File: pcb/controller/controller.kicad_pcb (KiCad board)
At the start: 2 copper layers, 100 x 40 mm, 27 parts, among them J1 Conn_01x02, J10 USB_C_Receptacle_USB2.0_16P, J2 Conn_01x02, J3 Conn_01x02, J4 Conn_01x02, J5 Conn_01x02, J6 Conn_01x02, J7 Conn_01x02, J8 RJ45, U2 AP2112K-3.3

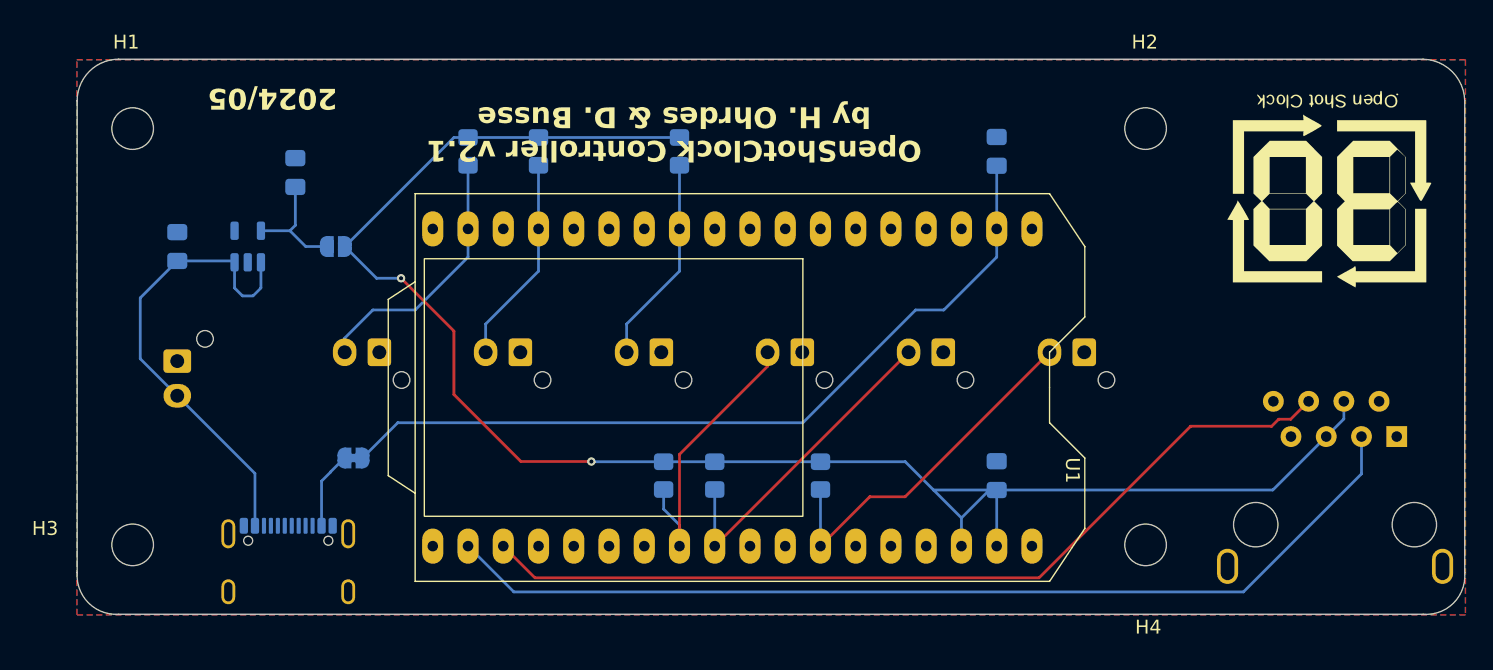
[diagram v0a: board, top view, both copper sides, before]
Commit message: fix missing 5V connection in controller PCB, when USB-C is not used, bump to v2.2
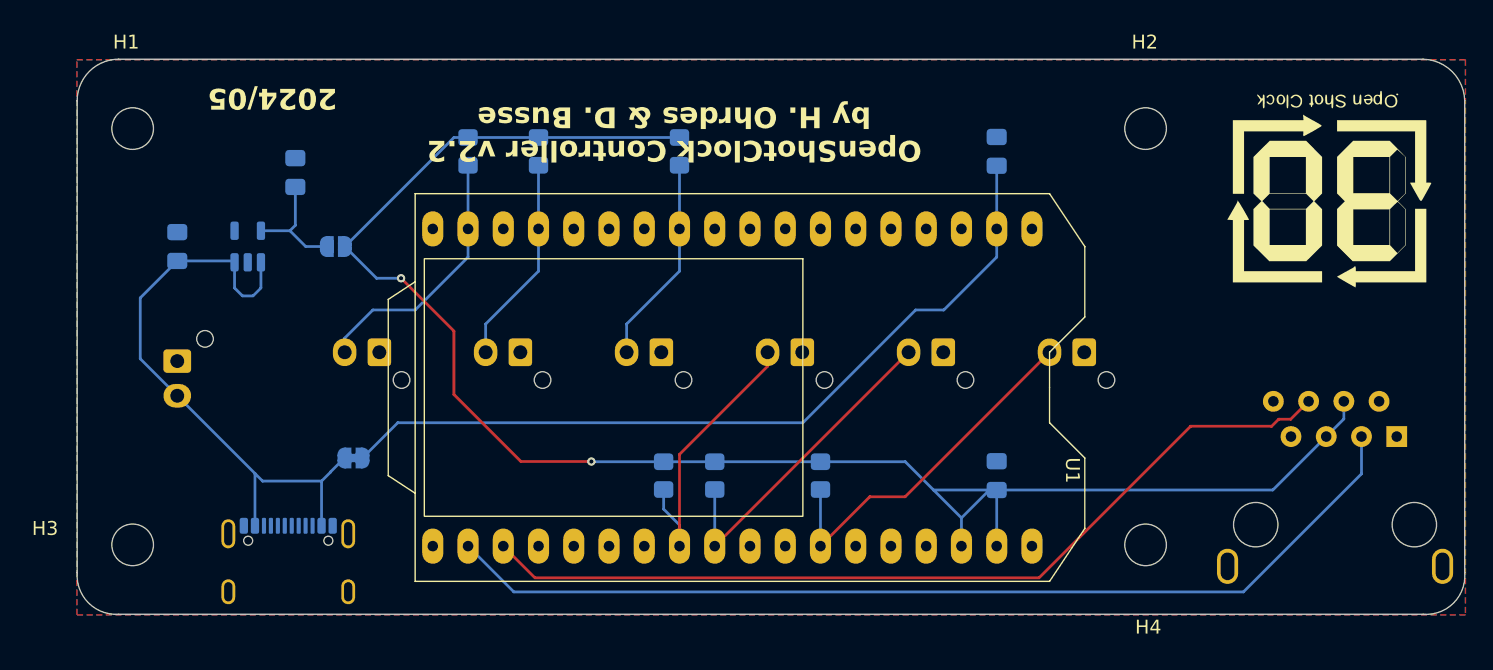
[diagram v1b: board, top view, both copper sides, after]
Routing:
- net 5V_IN: track 39.4 -> 44.5 mm
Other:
- board text added: "OpenShotClock Controller v2.2"
- board text added: "OpenShotClock Controller v2.2 by H. Ohrdes & D. Busse"
- board text removed: "OpenShotClock Controller v2.1"
- board text removed: "OpenShotClock Controller v2.1 by H. Ohrdes & D. Busse"
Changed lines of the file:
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@@
 		)
 	)
-	(gr_text "OpenShotClock Controller v2.1"
+	(gr_text "OpenShotClock Controller v2.2"
 		(at 87.122 51.943 180)
 		(layer "B.SilkS")
@@
 		)
 	)
-	(gr_text "OpenShotClock Controller v2.1\nby H. Ohrdes & D. Busse"
+	(gr_text "OpenShotClock Controller v2.2\nby H. Ohrdes & D. Busse"
 		(at 105.029 55.372 180)
 		(layer "F.SilkS")
@@
 	)
 	(segment
+		(start 75.366 80.406)
+		(end 79.614 80.406)
+		(width 0.2)
+		(layer "B.Cu")
+		(net 33)
+	)
+	(segment
 		(start 80.264 79.756)
 		(end 80.264 79.741)
@@
 		(width 0.2)
 		(layer "B.Cu")
+		(net 33)
+	)
+	(segment
+		(start 74.814 79.854)
+		(end 75.366 80.406)
+		(width 0.2)
+		(layer "B.Cu")

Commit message: update controller PCB: wider traces, fix missing trace on V+, add comments, update gerber files
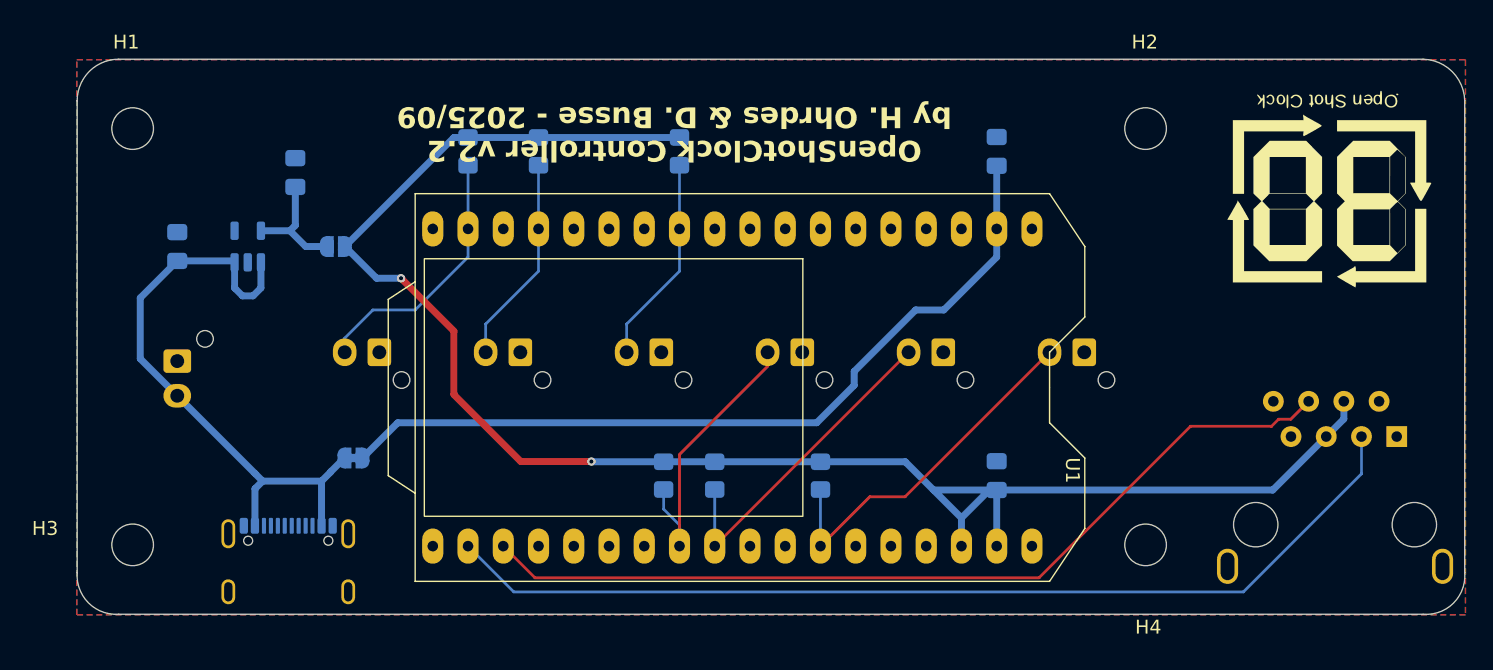
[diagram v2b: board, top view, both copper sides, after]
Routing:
- net 5V: track 58.3 -> 58.9 mm
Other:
- board text added: "OpenShotClock Controller v2.2 by H. Ohrdes & D. Busse - 2025/09"
- board text added: "connect to use external LDO"
- board text added: "disconnect if external LDO is used"
- board text removed: "2024/05"
- board text removed: "OpenShotClock Controller v2.2 by H. Ohrdes & D. Busse"
